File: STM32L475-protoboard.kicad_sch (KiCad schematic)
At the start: 91 parts, among them J1 USB_HEADER, J10 BOOT_MODE, J11 PAD_PB4, J12 PAD_PB5, J13 PAD_PC4, J14 PAD_PC5, J15 PAD_GND, J16 Conn_02x20_Odd_Even, J17 3v3-hdr, J3 DCin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

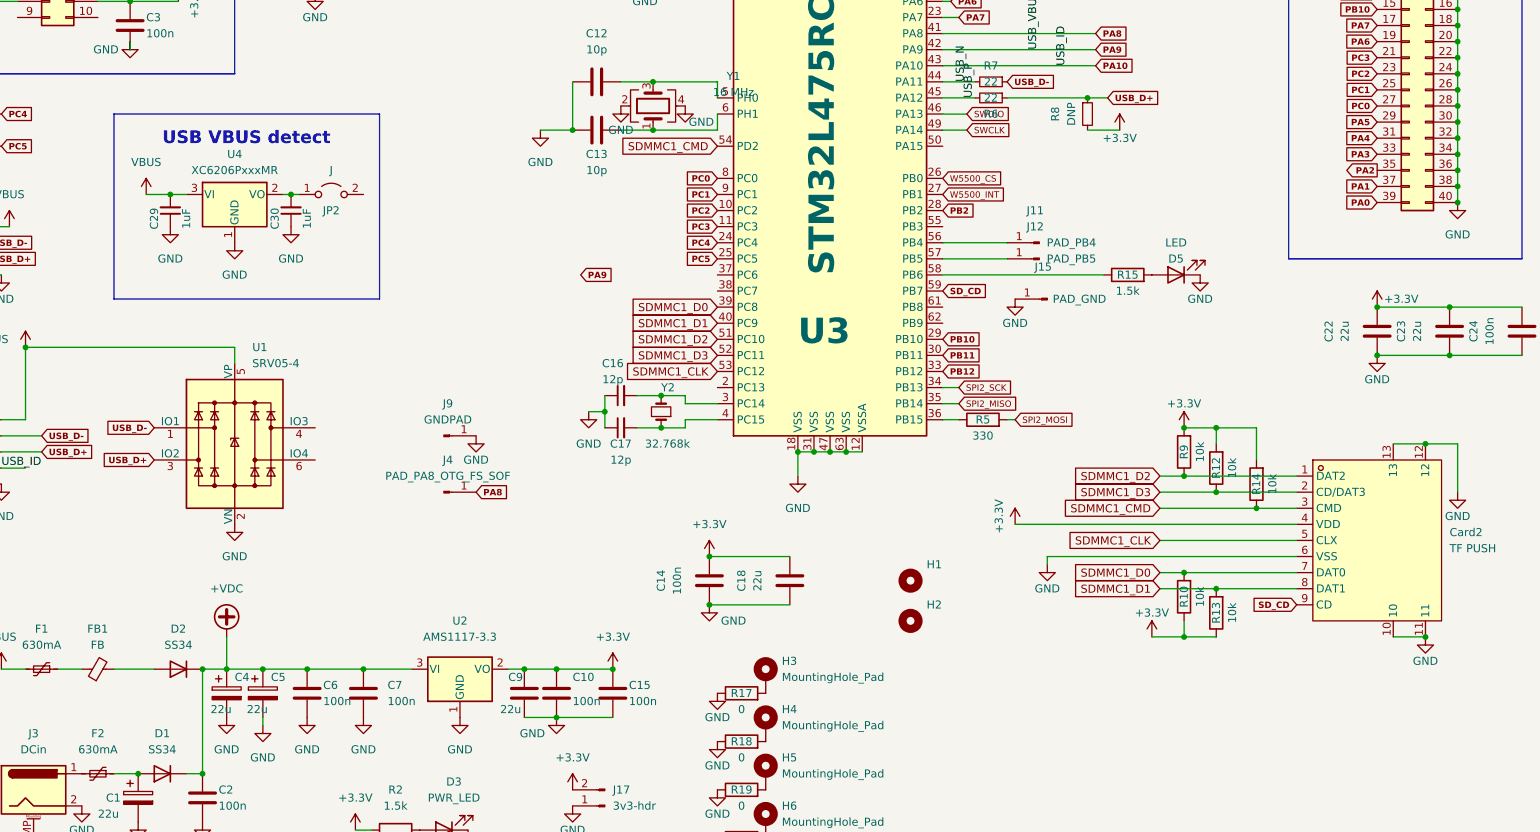
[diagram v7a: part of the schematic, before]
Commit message: fixed a couple of DRC errors
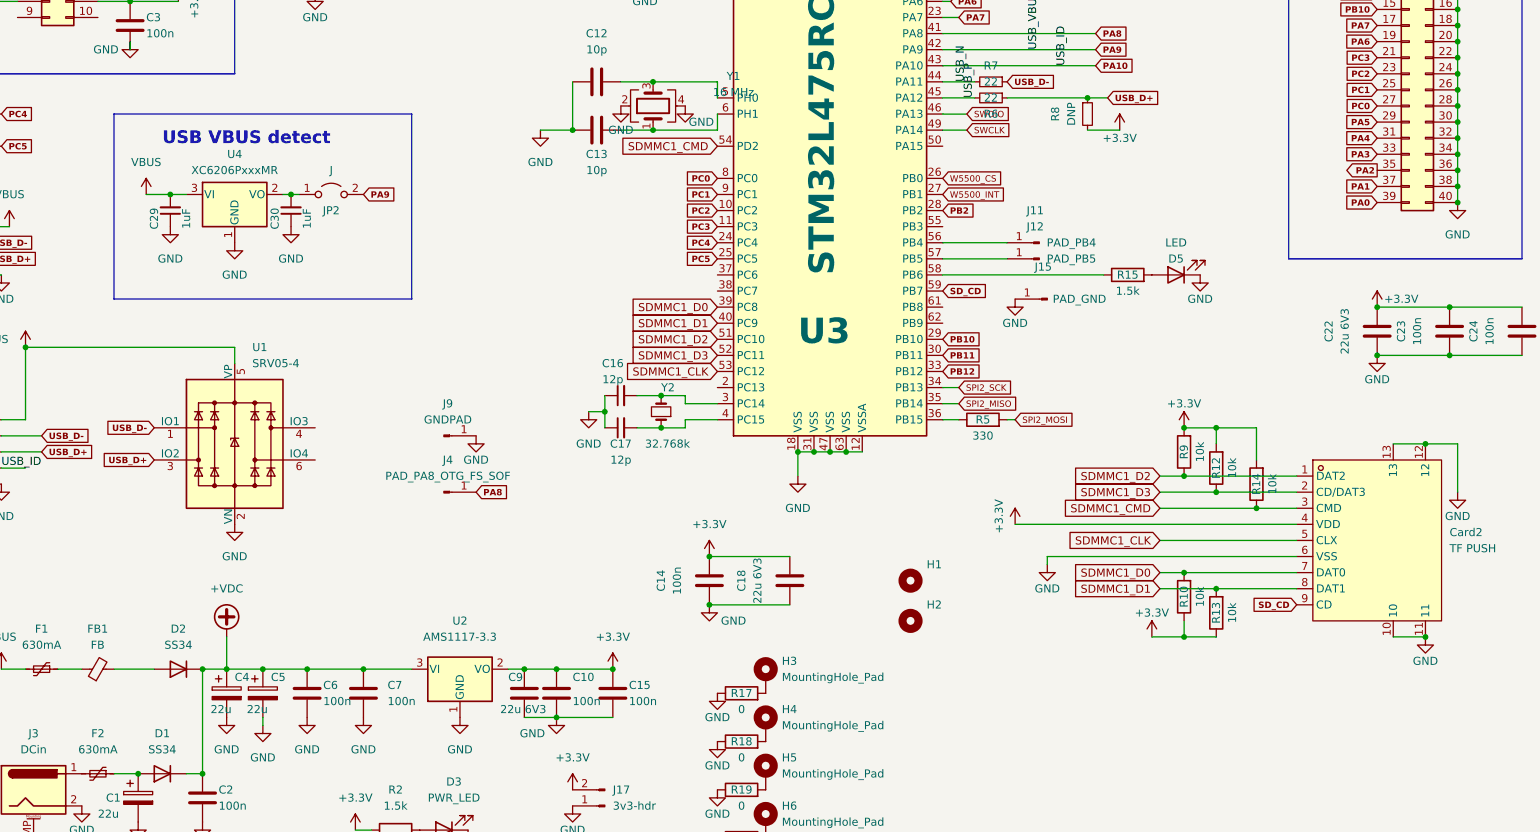
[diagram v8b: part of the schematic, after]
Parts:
- C18, C22, C9: value 22u -> 22u 6V3; footprint Capacitor_SMD:C_0805_2012Metric -> Capacitor_SMD:C_0603_1608Metric; LCSC C45783 -> C59461
- C23: value 22u -> 100n
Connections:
- net PA9: now also JP2.2 (B)
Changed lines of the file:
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@@
     (fill (type none))
   )
-  (rectangle (start 49.53 77.47) (end 91.44 106.68)
+  (rectangle (start 49.53 77.47) (end 96.52 106.68)
     (stroke (width 0) (type default))
     (fill (type none))
@@
     )
   )
-  (global_label "PA9" (shape input) (at 123.19 102.87 0) (fields_autoplaced)
+  (global_label "PA9" (shape input) (at 88.9 90.17 0) (fields_autoplaced)
     (effects (font (size 1 1) (thickness 0.2) bold) (justify left))
-    (property "Intersheetrefs" "${INTERSHEET_REFS}" (at 128.0495 102.77 0)
+    (property "Intersheetrefs" "${INTERSHEET_REFS}" (at 93.7595 90.07 0)
       (effects (font (size 1 1) (thickness 0.2) bold) (justify left) hide)
     )
@@
       (effects (font (size 1.27 1.27)))
     )
-    (property "Value" "22u" (at 255.27 111.76 90)
+    (property "Value" "100n" (at 255.27 111.76 90)
       (effects (font (size 1.27 1.27)))
     )
@@
       (effects (font (size 1.27 1.27)))
     )
-    (property "Value" "22u" (at 151.13 151.13 90)
+    (property "Value" "22u 6V3" (at 151.13 151.13 90)
       (effects (font (size 1.27 1.27)))
     )
-    (property "Footprint" "Capacitor_SMD:C_0805_2012Metric" (at 155.2448 147.32 0)
+    (property "Footprint" "Capacitor_SMD:C_0603_1608Metric" (at 155.2448 147.32 0)
       (effects (font (size 1.27 1.27)) hide)
     )
@@
       (effects (font (size 1.27 1.27)) hide)
     )
-    (property "LCSC" "C45783" (at 156.21 151.13 0)
+    (property "LCSC" "C59461" (at 156.21 151.13 0)
       (effects (font (size 1.27 1.27)) hide)
     )
@@
       (effects (font (size 1.27 1.27)) (justify left))
     )
-    (property "Value" "22u" (at 110.49 171.45 0)
+    (property "Value" "22u 6V3" (at 110.49 171.45 0)
       (effects (font (size 1.27 1.27)) (justify left))
     )
-    (property "Footprint" "Capacitor_SMD:C_0805_2012Metric" (at 115.2652 172.72 0)
+    (property "Footprint" "Capacitor_SMD:C_0603_1608Metric" (at 115.2652 172.72 0)
       (effects (font (size 1.27 1.27)) hide)
     )
@@
       (effects (font (size 1.27 1.27)) hide)
     )
-    (property "LCSC" "C45783" (at 114.3 168.91 0)
+    (property "LCSC" "C59461" (at 114.3 168.91 0)
       (effects (font (size 1.27 1.27)) hide)
     )
@@
       (effects (font (size 1.27 1.27)))
     )
-    (property "Value" "22u" (at 243.84 111.76 90)
+    (property "Value" "22u 6V3" (at 243.84 111.76 90)
       (effects (font (size 1.27 1.27)))
     )
-    (property "Footprint" "Capacitor_SMD:C_0805_2012Metric" (at 247.9548 107.95 0)
+    (property "Footprint" "Capacitor_SMD:C_0603_1608Metric" (at 247.9548 107.95 0)
       (effects (font (size 1.27 1.27)) hide)
     )
@@
       (effects (font (size 1.27 1.27)) hide)
     )
-    (property "LCSC" "C45783" (at 248.92 111.76 0)
+    (property "LCSC" "C59461" (at 248.92 111.76 0)
       (effects (font (size 1.27 1.27)) hide)
     )
